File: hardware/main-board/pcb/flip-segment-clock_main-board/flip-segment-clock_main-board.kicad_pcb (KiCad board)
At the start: 2 copper layers, 29.4 x 23 mm, 13 parts, among them IC1 STM32G071CBT6, IC2 DS3231MZ+TRL, IC3 TPS62177DQCR, J1 Barrel_Jack

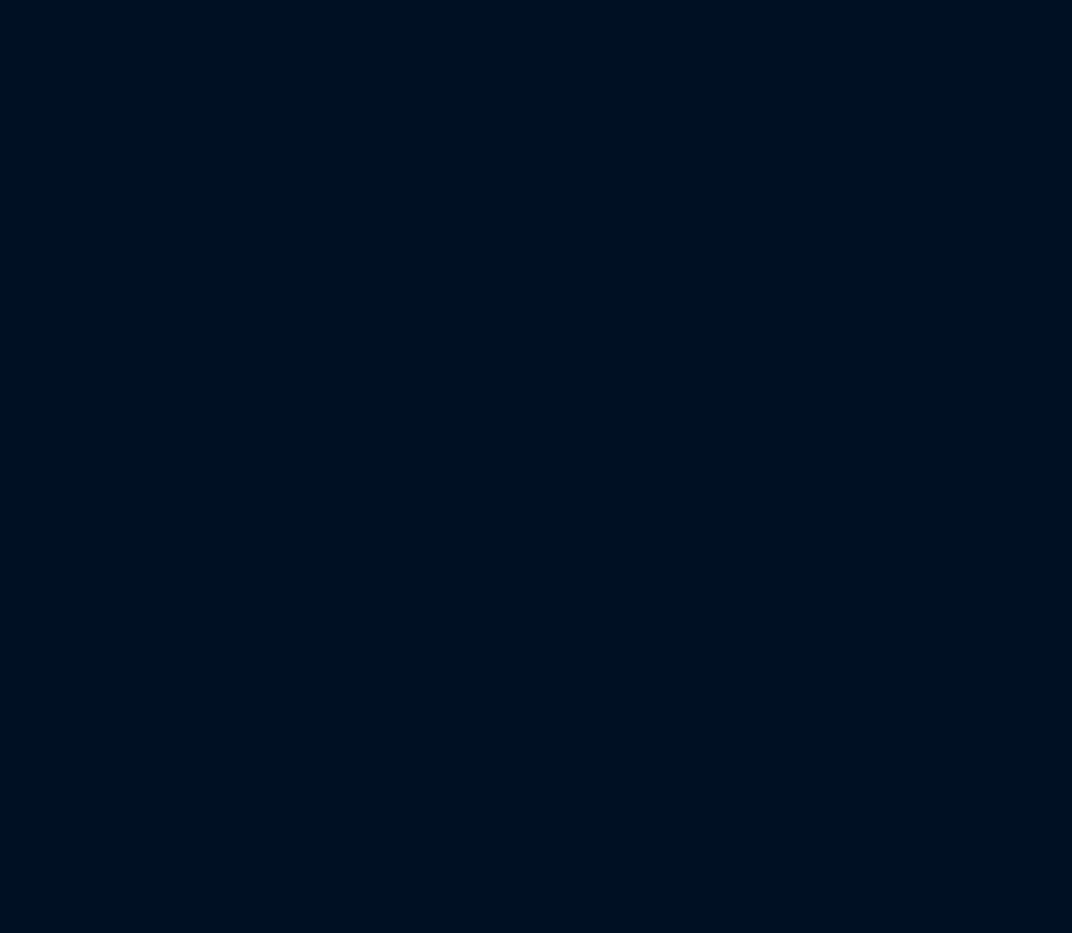
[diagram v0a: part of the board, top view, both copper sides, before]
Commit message: Segment driver update
Continuing refinement of segment driver design, settle on per digit vbb isolation, no overlapping between a3909
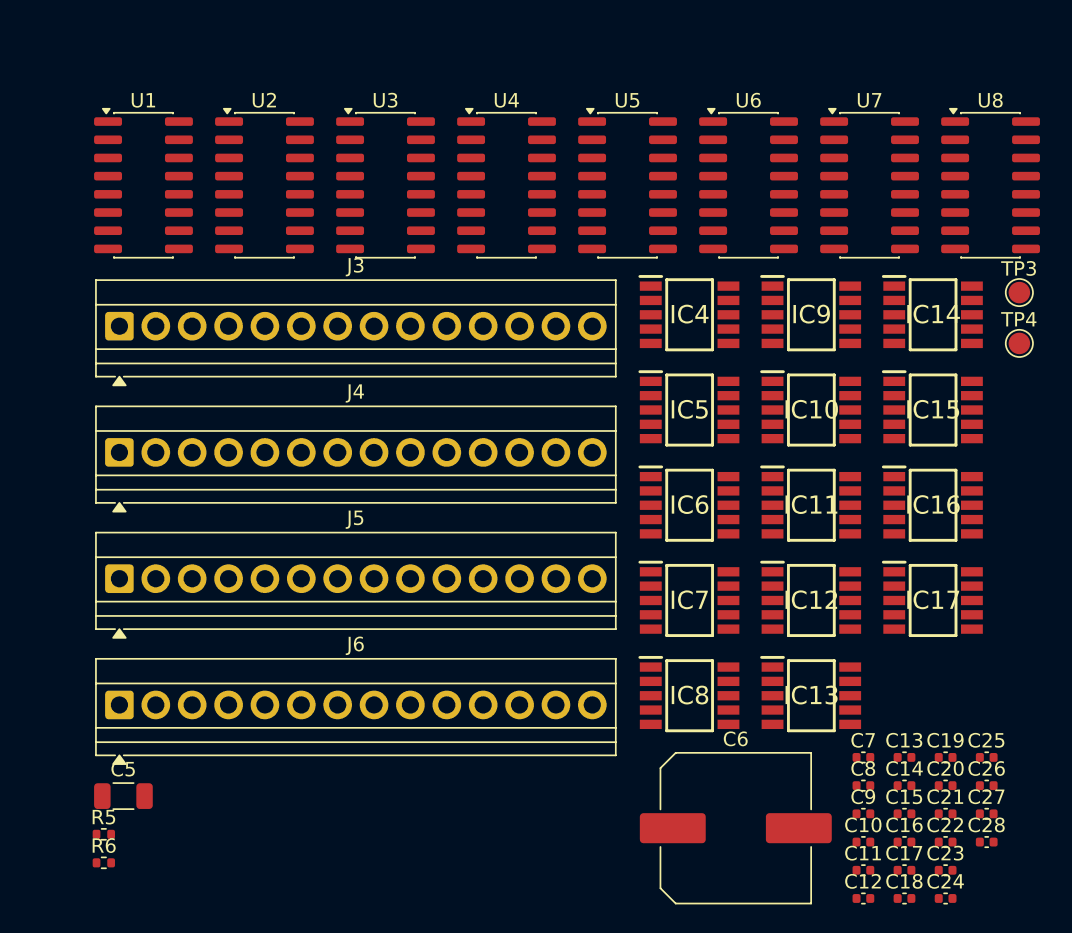
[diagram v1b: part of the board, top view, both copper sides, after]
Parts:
- added C10: 100 nF, Capacitor_SMD:C_0402_1005Metric, F.Cu at (235.7, 118.8)
- added C11: 100 nF, Capacitor_SMD:C_0402_1005Metric, F.Cu at (235.7, 120.7)
- added C12: 100 nF, Capacitor_SMD:C_0402_1005Metric, F.Cu at (235.7, 122.7)
- added C13: 100 nF, Capacitor_SMD:C_0402_1005Metric, F.Cu at (238.5, 112.8)
- added C14: 100 nF, Capacitor_SMD:C_0402_1005Metric, F.Cu at (238.5, 114.8)
- added C15: 100 nF, Capacitor_SMD:C_0402_1005Metric, F.Cu at (238.5, 116.8)
- added C16: 100 nF, Capacitor_SMD:C_0402_1005Metric, F.Cu at (238.5, 118.8)
- added C17: 100 nF, Capacitor_SMD:C_0402_1005Metric, F.Cu at (238.5, 120.7)
- added C18: 100 nF, Capacitor_SMD:C_0402_1005Metric, F.Cu at (238.5, 122.7)
- added C19: 100 nF, Capacitor_SMD:C_0402_1005Metric, F.Cu at (241.4, 112.8)
- added C20: 100 nF, Capacitor_SMD:C_0402_1005Metric, F.Cu at (241.4, 114.8)
- added C21: 100 nF, Capacitor_SMD:C_0402_1005Metric, F.Cu at (241.4, 116.8)
- added C22: 100 nF, Capacitor_SMD:C_0402_1005Metric, F.Cu at (241.4, 118.8)
- added C23: 100 nF, Capacitor_SMD:C_0402_1005Metric, F.Cu at (241.4, 120.7)
- added C24: 100 nF, Capacitor_SMD:C_0402_1005Metric, F.Cu at (241.4, 122.7)
- added C25: 100 nF, Capacitor_SMD:C_0402_1005Metric, F.Cu at (244.3, 112.8)
- added C26: 100 nF, Capacitor_SMD:C_0402_1005Metric, F.Cu at (244.3, 114.8)
- added C27: 100 nF, Capacitor_SMD:C_0402_1005Metric, F.Cu at (244.3, 116.8)
- added C28: 100 nF, Capacitor_SMD:C_0402_1005Metric, F.Cu at (244.3, 118.8)
- added C5: 10 uF, Capacitor_SMD:C_1206_3216Metric, F.Cu at (184.0, 115.5)
- added C6: 560 uF, Capacitor_SMD:C_Elec_10x10.2, F.Cu at (226.8, 117.8)
- added C7: 100 nF, Capacitor_SMD:C_0402_1005Metric, F.Cu at (235.7, 112.8)
- added C8: 100 nF, Capacitor_SMD:C_0402_1005Metric, F.Cu at (235.7, 114.8)
- added C9: 100 nF, Capacitor_SMD:C_0402_1005Metric, F.Cu at (235.7, 116.8)
- added IC10: A3909GLNTR-T, SamacSys_Parts:SOP100P600X175-10N, F.Cu at (232.0, 88.6)
- added IC11: A3909GLNTR-T, SamacSys_Parts:SOP100P600X175-10N, F.Cu at (232.0, 95.2)
- added IC12: A3909GLNTR-T, SamacSys_Parts:SOP100P600X175-10N, F.Cu at (232.0, 101.9)
- added IC13: A3909GLNTR-T, SamacSys_Parts:SOP100P600X175-10N, F.Cu at (232.0, 108.5)
- added IC14: A3909GLNTR-T, SamacSys_Parts:SOP100P600X175-10N, F.Cu at (240.5, 81.9)
- added IC15: A3909GLNTR-T, SamacSys_Parts:SOP100P600X175-10N, F.Cu at (240.5, 88.6)
- added IC16: A3909GLNTR-T, SamacSys_Parts:SOP100P600X175-10N, F.Cu at (240.5, 95.2)
- added IC17: A3909GLNTR-T, SamacSys_Parts:SOP100P600X175-10N, F.Cu at (240.5, 101.9)
- added IC4: A3909GLNTR-T, SamacSys_Parts:SOP100P600X175-10N, F.Cu at (223.5, 81.9)
- added IC5: A3909GLNTR-T, SamacSys_Parts:SOP100P600X175-10N, F.Cu at (223.5, 88.6)
- added IC6: A3909GLNTR-T, SamacSys_Parts:SOP100P600X175-10N, F.Cu at (223.5, 95.2)
- added IC7: A3909GLNTR-T, SamacSys_Parts:SOP100P600X175-10N, F.Cu at (223.5, 101.9)
- added IC8: A3909GLNTR-T, SamacSys_Parts:SOP100P600X175-10N, F.Cu at (223.5, 108.5)
- added IC9: A3909GLNTR-T, SamacSys_Parts:SOP100P600X175-10N, F.Cu at (232.0, 81.9)
- added J3: Digit 1, TerminalBlock:TerminalBlock_Xinya_XY308-2.54-14P_1x14_P2.54mm_Horizontal, F.Cu at (183.7, 82.7)
- added J4: Digit 2, TerminalBlock:TerminalBlock_Xinya_XY308-2.54-14P_1x14_P2.54mm_Horizontal, F.Cu at (183.7, 91.5)
- added J5: Digit 3, TerminalBlock:TerminalBlock_Xinya_XY308-2.54-14P_1x14_P2.54mm_Horizontal, F.Cu at (183.7, 100.4)
- added J6: Digit 4, TerminalBlock:TerminalBlock_Xinya_XY308-2.54-14P_1x14_P2.54mm_Horizontal, F.Cu at (183.7, 109.2)
- added R5: 100K, Resistor_SMD:R_0402_1005Metric, F.Cu at (182.6, 118.2)
- added R6: 100K, Resistor_SMD:R_0402_1005Metric, F.Cu at (182.6, 120.2)
- added TP3: SER, TestPoint:TestPoint_Pad_D1.5mm, F.Cu at (246.6, 80.4)
- added TP4: 12v, TestPoint:TestPoint_Pad_D1.5mm, F.Cu at (246.6, 83.9)
- added U1: 74HC595, Package_SO:SOIC-16_3.9x9.9mm_P1.27mm, F.Cu at (185.4, 72.9)
- added U2: 74HC595, Package_SO:SOIC-16_3.9x9.9mm_P1.27mm, F.Cu at (193.8, 72.9)
- added U3: 74HC595, Package_SO:SOIC-16_3.9x9.9mm_P1.27mm, F.Cu at (202.3, 72.9)
- added U4: 74HC595, Package_SO:SOIC-16_3.9x9.9mm_P1.27mm, F.Cu at (210.7, 72.9)
- added U5: 74HC595, Package_SO:SOIC-16_3.9x9.9mm_P1.27mm, F.Cu at (219.2, 72.9)
- added U6: 74HC595, Package_SO:SOIC-16_3.9x9.9mm_P1.27mm, F.Cu at (227.6, 72.9)
- added U7: 74HC595, Package_SO:SOIC-16_3.9x9.9mm_P1.27mm, F.Cu at (236.1, 72.9)
- added U8: 74HC595, Package_SO:SOIC-16_3.9x9.9mm_P1.27mm, F.Cu at (244.5, 72.9)
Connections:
- net +12V renamed VBB
- net SCL renamed SCL_RTC
- net SDA renamed SDA_RTC

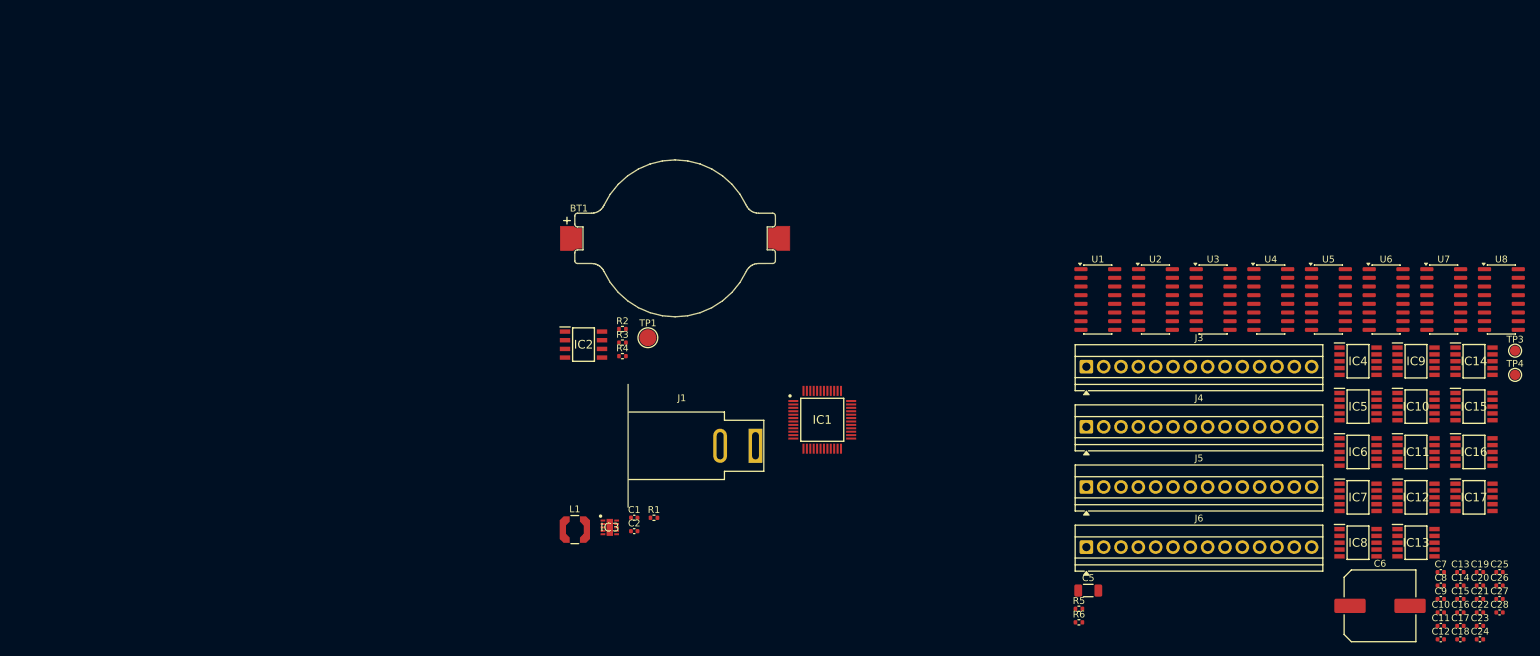
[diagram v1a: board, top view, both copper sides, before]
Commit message: Finalizing design of digit VBB isolation
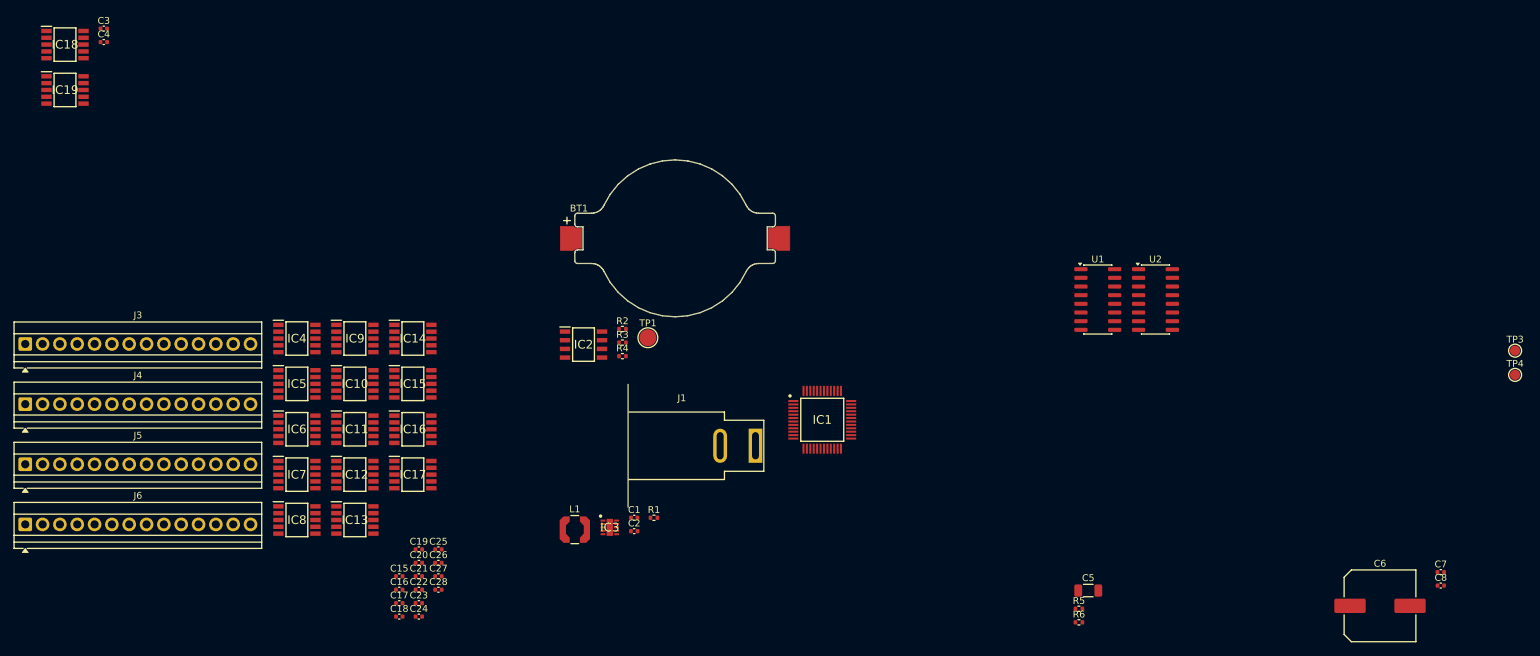
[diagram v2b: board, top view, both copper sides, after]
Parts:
- removed C10, C11, C12, C13, C14, C9: 100 nF, Capacitor_SMD:C_0402_1005Metric
- removed U3, U4, U5, U6, U7, U8: 74HC595, Package_SO:SOIC-16_3.9x9.9mm_P1.27mm
- added C3: 100 nF, Capacitor_SMD:C_0402_1005Metric, F.Cu at (39.7, 33.2)
- added C4: 100 nF, Capacitor_SMD:C_0402_1005Metric, F.Cu at (39.7, 35.1)
- added IC18: A3909GLNTR-T, SamacSys_Parts:SOP100P600X175-10N, F.Cu at (34.0, 35.5)
- added IC19: A3909GLNTR-T, SamacSys_Parts:SOP100P600X175-10N, F.Cu at (34.0, 42.2)
- moved C15 155.6 mm to (83.0, 113.5)
- moved C16 155.6 mm to (83.0, 115.4)
- moved C17 155.6 mm to (83.0, 117.4)
- moved C18 155.6 mm to (83.0, 119.4)
- moved C19 155.6 mm to (85.9, 109.5)
- moved C20 155.6 mm to (85.9, 111.5)
- moved C21 155.6 mm to (85.9, 113.5)
- moved C22 155.6 mm to (85.9, 115.4)
- moved C23 155.6 mm to (85.9, 117.4)
- moved C24 155.6 mm to (85.9, 119.4)
- moved C25 155.6 mm to (88.7, 109.5)
- moved C26 155.6 mm to (88.7, 111.5)
- moved C27 155.6 mm to (88.7, 113.5)
- moved C28 155.6 mm to (88.7, 115.4)
- moved IC10 155.6 mm to (76.5, 85.2)
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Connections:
- C1 pad 2: VBB -> +12V
- C15 pad 2: VBB -> DIG1
- C16 pad 2: VBB -> DIG1
- C17 pad 2: VBB -> DIG1
- C18 pad 2: VBB -> DIG2
- C19 pad 2: VBB -> DIG2
- C20 pad 2: VBB -> DIG2
- C21 pad 2: VBB -> DIG2
- C22 pad 2: VBB -> DIG3
- C23 pad 2: VBB -> DIG3
- C24 pad 2: VBB -> DIG3
- C25 pad 2: VBB -> DIG4
- C26 pad 2: VBB -> DIG4
- C27 pad 2: VBB -> DIG4
- C28 pad 2: VBB -> DIG4
- C5 pad 2: VBB -> +12V
- C6 pad 1: VBB -> +12V
- IC10 pad 1: unconnected-(IC10-IN1-Pad1) -> F3
- IC10 pad 10: unconnected-(IC10-OUT1-Pad10) -> Net-(IC10-OUT1)
- IC10 pad 2: unconnected-(IC10-IN2-Pad2) -> F4
- IC10 pad 3: VBB -> DIG2
- IC10 pad 4: unconnected-(IC10-IN3-Pad4) -> G1
- IC10 pad 5: unconnected-(IC10-IN4-Pad5) -> G2
- IC10 pad 6: unconnected-(IC10-OUT4-Pad6) -> Net-(IC10-OUT4)
- IC10 pad 7: unconnected-(IC10-OUT3-Pad7) -> Net-(IC10-OUT3)
- IC10 pad 9: unconnected-(IC10-OUT2-Pad9) -> Net-(IC10-OUT2)
- IC11 pad 1: unconnected-(IC11-IN1-Pad1) -> A1
- IC11 pad 10: unconnected-(IC11-OUT1-Pad10) -> Net-(IC11-OUT1)
- IC11 pad 2: unconnected-(IC11-IN2-Pad2) -> A2
- IC11 pad 3: VBB -> DIG3
- IC11 pad 4: unconnected-(IC11-IN3-Pad4) -> B3
- IC11 pad 5: unconnected-(IC11-IN4-Pad5) -> B4
- IC11 pad 6: unconnected-(IC11-OUT4-Pad6) -> Net-(IC11-OUT4)
- IC11 pad 7: unconnected-(IC11-OUT3-Pad7) -> Net-(IC11-OUT3)
- IC11 pad 9: unconnected-(IC11-OUT2-Pad9) -> Net-(IC11-OUT2)
- IC12 pad 1: unconnected-(IC12-IN1-Pad1) -> C1
- IC12 pad 10: unconnected-(IC12-OUT1-Pad10) -> Net-(IC12-OUT1)
- IC12 pad 2: unconnected-(IC12-IN2-Pad2) -> C2
- IC12 pad 3: VBB -> DIG3
- IC12 pad 4: unconnected-(IC12-IN3-Pad4) -> D3
- IC12 pad 5: unconnected-(IC12-IN4-Pad5) -> D4
- IC12 pad 6: unconnected-(IC12-OUT4-Pad6) -> Net-(IC12-OUT4)
- IC12 pad 7: unconnected-(IC12-OUT3-Pad7) -> Net-(IC12-OUT3)
- IC12 pad 9: unconnected-(IC12-OUT2-Pad9) -> Net-(IC12-OUT2)
- IC13 pad 1: unconnected-(IC13-IN1-Pad1) -> E1
- IC13 pad 10: unconnected-(IC13-OUT1-Pad10) -> Net-(IC13-OUT1)
- IC13 pad 2: unconnected-(IC13-IN2-Pad2) -> E2
- IC13 pad 3: VBB -> DIG3
- IC13 pad 4: unconnected-(IC13-IN3-Pad4) -> F3
- IC13 pad 5: unconnected-(IC13-IN4-Pad5) -> F4
- IC13 pad 6: unconnected-(IC13-OUT4-Pad6) -> Net-(IC13-OUT4)
- IC13 pad 7: unconnected-(IC13-OUT3-Pad7) -> Net-(IC13-OUT3)
- IC13 pad 9: unconnected-(IC13-OUT2-Pad9) -> Net-(IC13-OUT2)
- IC14 pad 1: unconnected-(IC14-IN1-Pad1) -> GND
- IC14 pad 2: unconnected-(IC14-IN2-Pad2) -> GND
- IC14 pad 3: VBB -> DIG4
- IC14 pad 4: unconnected-(IC14-IN3-Pad4) -> A1
- IC14 pad 5: unconnected-(IC14-IN4-Pad5) -> A2
- IC14 pad 6: unconnected-(IC14-OUT4-Pad6) -> Net-(IC14-OUT4)
- IC14 pad 7: unconnected-(IC14-OUT3-Pad7) -> Net-(IC14-OUT3)
- IC15 pad 1: unconnected-(IC15-IN1-Pad1) -> B3
- IC15 pad 10: unconnected-(IC15-OUT1-Pad10) -> Net-(IC15-OUT1)
- IC15 pad 2: unconnected-(IC15-IN2-Pad2) -> B4
- IC15 pad 3: VBB -> DIG4
- IC15 pad 4: unconnected-(IC15-IN3-Pad4) -> C1
- IC15 pad 5: unconnected-(IC15-IN4-Pad5) -> C2
- IC15 pad 6: unconnected-(IC15-OUT4-Pad6) -> Net-(IC15-OUT4)
- IC15 pad 7: unconnected-(IC15-OUT3-Pad7) -> Net-(IC15-OUT3)
- IC15 pad 9: unconnected-(IC15-OUT2-Pad9) -> Net-(IC15-OUT2)
- IC16 pad 1: unconnected-(IC16-IN1-Pad1) -> D3
- IC16 pad 10: unconnected-(IC16-OUT1-Pad10) -> Net-(IC16-OUT1)
- IC16 pad 2: unconnected-(IC16-IN2-Pad2) -> D4
- IC16 pad 3: VBB -> DIG4
- IC16 pad 4: unconnected-(IC16-IN3-Pad4) -> E1
- IC16 pad 5: unconnected-(IC16-IN4-Pad5) -> E2
- IC16 pad 6: unconnected-(IC16-OUT4-Pad6) -> Net-(IC16-OUT4)
- IC16 pad 7: unconnected-(IC16-OUT3-Pad7) -> Net-(IC16-OUT3)
- IC16 pad 9: unconnected-(IC16-OUT2-Pad9) -> Net-(IC16-OUT2)
- IC17 pad 1: unconnected-(IC17-IN1-Pad1) -> F3
- IC17 pad 10: unconnected-(IC17-OUT1-Pad10) -> Net-(IC17-OUT1)
- IC17 pad 2: unconnected-(IC17-IN2-Pad2) -> F4
- IC17 pad 3: VBB -> DIG4
- IC17 pad 4: unconnected-(IC17-IN3-Pad4) -> G1
- IC17 pad 5: unconnected-(IC17-IN4-Pad5) -> G2
- IC17 pad 6: unconnected-(IC17-OUT4-Pad6) -> Net-(IC17-OUT4)
- IC17 pad 7: unconnected-(IC17-OUT3-Pad7) -> Net-(IC17-OUT3)
- IC17 pad 9: unconnected-(IC17-OUT2-Pad9) -> Net-(IC17-OUT2)
- IC3 pad 2: VBB -> +12V
- IC3 pad 3: VBB -> +12V
- IC4 pad 1: unconnected-(IC4-IN1-Pad1) -> A1
- IC4 pad 10: unconnected-(IC4-OUT1-Pad10) -> Net-(IC4-OUT1)
- IC4 pad 2: unconnected-(IC4-IN2-Pad2) -> A2
- IC4 pad 3: VBB -> DIG1
- IC4 pad 4: unconnected-(IC4-IN3-Pad4) -> B3
- IC4 pad 5: unconnected-(IC4-IN4-Pad5) -> B4
- IC4 pad 6: unconnected-(IC4-OUT4-Pad6) -> Net-(IC4-OUT4)
- IC4 pad 7: unconnected-(IC4-OUT3-Pad7) -> Net-(IC4-OUT3)
- IC4 pad 9: unconnected-(IC4-OUT2-Pad9) -> Net-(IC4-OUT2)
- IC5 pad 1: unconnected-(IC5-IN1-Pad1) -> C1
- IC5 pad 10: unconnected-(IC5-OUT1-Pad10) -> Net-(IC5-OUT1)
- IC5 pad 2: unconnected-(IC5-IN2-Pad2) -> C2
- IC5 pad 3: VBB -> DIG1
- IC5 pad 4: unconnected-(IC5-IN3-Pad4) -> D3
- IC5 pad 5: unconnected-(IC5-IN4-Pad5) -> D4
- IC5 pad 6: unconnected-(IC5-OUT4-Pad6) -> Net-(IC5-OUT4)
- IC5 pad 7: unconnected-(IC5-OUT3-Pad7) -> Net-(IC5-OUT3)
- IC5 pad 9: unconnected-(IC5-OUT2-Pad9) -> Net-(IC5-OUT2)
- IC6 pad 1: unconnected-(IC6-IN1-Pad1) -> E1
- IC6 pad 10: unconnected-(IC6-OUT1-Pad10) -> Net-(IC6-OUT1)
- IC6 pad 2: unconnected-(IC6-IN2-Pad2) -> E2
- IC6 pad 3: VBB -> DIG1
- IC6 pad 4: unconnected-(IC6-IN3-Pad4) -> F3
- IC6 pad 5: unconnected-(IC6-IN4-Pad5) -> F4
- IC6 pad 6: unconnected-(IC6-OUT4-Pad6) -> Net-(IC6-OUT4)
- IC6 pad 7: unconnected-(IC6-OUT3-Pad7) -> Net-(IC6-OUT3)
- IC6 pad 9: unconnected-(IC6-OUT2-Pad9) -> Net-(IC6-OUT2)
- IC7 pad 1: unconnected-(IC7-IN1-Pad1) -> GND
- IC7 pad 2: unconnected-(IC7-IN2-Pad2) -> GND
- IC7 pad 3: VBB -> DIG2
- IC7 pad 4: unconnected-(IC7-IN3-Pad4) -> A1
- IC7 pad 5: unconnected-(IC7-IN4-Pad5) -> A2
- IC7 pad 6: unconnected-(IC7-OUT4-Pad6) -> Net-(IC7-OUT4)
- IC7 pad 7: unconnected-(IC7-OUT3-Pad7) -> Net-(IC7-OUT3)
- IC8 pad 1: unconnected-(IC8-IN1-Pad1) -> B3
- IC8 pad 10: unconnected-(IC8-OUT1-Pad10) -> Net-(IC8-OUT1)
- IC8 pad 2: unconnected-(IC8-IN2-Pad2) -> B4
- IC8 pad 3: VBB -> DIG2
- IC8 pad 4: unconnected-(IC8-IN3-Pad4) -> C1
- IC8 pad 5: unconnected-(IC8-IN4-Pad5) -> C2
- IC8 pad 6: unconnected-(IC8-OUT4-Pad6) -> Net-(IC8-OUT4)
- IC8 pad 7: unconnected-(IC8-OUT3-Pad7) -> Net-(IC8-OUT3)
- IC8 pad 9: unconnected-(IC8-OUT2-Pad9) -> Net-(IC8-OUT2)
- IC9 pad 1: unconnected-(IC9-IN1-Pad1) -> D3
- IC9 pad 10: unconnected-(IC9-OUT1-Pad10) -> Net-(IC9-OUT1)
- IC9 pad 2: unconnected-(IC9-IN2-Pad2) -> D4
- IC9 pad 3: VBB -> DIG2
- IC9 pad 4: unconnected-(IC9-IN3-Pad4) -> E1
- IC9 pad 5: unconnected-(IC9-IN4-Pad5) -> E2
- IC9 pad 6: unconnected-(IC9-OUT4-Pad6) -> Net-(IC9-OUT4)
- IC9 pad 7: unconnected-(IC9-OUT3-Pad7) -> Net-(IC9-OUT3)
- IC9 pad 9: unconnected-(IC9-OUT2-Pad9) -> Net-(IC9-OUT2)
- J1 pad 1: VBB -> +12V
- J3 pad 1: unconnected-(J3-Pin_1-Pad1) -> Net-(IC4-OUT1)
- J3 pad 10: unconnected-(J3-Pin_10-Pad10) -> Net-(IC6-OUT2)
- J3 pad 11: unconnected-(J3-Pin_11-Pad11) -> Net-(IC6-OUT3)
- J3 pad 12: unconnected-(J3-Pin_12-Pad12) -> Net-(IC6-OUT4)
- J3 pad 13: unconnected-(J3-Pin_13-Pad13) -> Net-(IC18-OUT1)
- J3 pad 14: unconnected-(J3-Pin_14-Pad14) -> Net-(IC18-OUT2)
- J3 pad 2: unconnected-(J3-Pin_2-Pad2) -> Net-(IC4-OUT2)
- J3 pad 3: unconnected-(J3-Pin_3-Pad3) -> Net-(IC4-OUT3)
- J3 pad 4: unconnected-(J3-Pin_4-Pad4) -> Net-(IC4-OUT4)
- J3 pad 5: unconnected-(J3-Pin_5-Pad5) -> Net-(IC5-OUT1)
- J3 pad 6: unconnected-(J3-Pin_6-Pad6) -> Net-(IC5-OUT2)
- J3 pad 7: unconnected-(J3-Pin_7-Pad7) -> Net-(IC5-OUT3)
- J3 pad 8: unconnected-(J3-Pin_8-Pad8) -> Net-(IC5-OUT4)
- J3 pad 9: unconnected-(J3-Pin_9-Pad9) -> Net-(IC6-OUT1)
- J4 pad 1: unconnected-(J4-Pin_1-Pad1) -> Net-(IC7-OUT3)
- J4 pad 10: unconnected-(J4-Pin_10-Pad10) -> Net-(IC9-OUT4)
- J4 pad 11: unconnected-(J4-Pin_11-Pad11) -> Net-(IC10-OUT1)
- J4 pad 12: unconnected-(J4-Pin_12-Pad12) -> Net-(IC10-OUT2)
- J4 pad 13: unconnected-(J4-Pin_13-Pad13) -> Net-(IC10-OUT3)
- J4 pad 14: unconnected-(J4-Pin_14-Pad14) -> Net-(IC10-OUT4)
- J4 pad 2: unconnected-(J4-Pin_2-Pad2) -> Net-(IC7-OUT4)
- J4 pad 3: unconnected-(J4-Pin_3-Pad3) -> Net-(IC8-OUT1)
- J4 pad 4: unconnected-(J4-Pin_4-Pad4) -> Net-(IC8-OUT2)
- J4 pad 5: unconnected-(J4-Pin_5-Pad5) -> Net-(IC8-OUT3)
- J4 pad 6: unconnected-(J4-Pin_6-Pad6) -> Net-(IC8-OUT4)
- J4 pad 7: unconnected-(J4-Pin_7-Pad7) -> Net-(IC9-OUT1)
- J4 pad 8: unconnected-(J4-Pin_8-Pad8) -> Net-(IC9-OUT2)
- J4 pad 9: unconnected-(J4-Pin_9-Pad9) -> Net-(IC9-OUT3)
- J5 pad 1: unconnected-(J5-Pin_1-Pad1) -> Net-(IC11-OUT1)
- J5 pad 10: unconnected-(J5-Pin_10-Pad10) -> Net-(IC13-OUT2)
- J5 pad 11: unconnected-(J5-Pin_11-Pad11) -> Net-(IC13-OUT3)
- J5 pad 12: unconnected-(J5-Pin_12-Pad12) -> Net-(IC13-OUT4)
- J5 pad 13: unconnected-(J5-Pin_13-Pad13) -> Net-(IC19-OUT1)
- J5 pad 14: unconnected-(J5-Pin_14-Pad14) -> Net-(IC19-OUT2)
- J5 pad 2: unconnected-(J5-Pin_2-Pad2) -> Net-(IC11-OUT2)
- J5 pad 3: unconnected-(J5-Pin_3-Pad3) -> Net-(IC11-OUT3)
- J5 pad 4: unconnected-(J5-Pin_4-Pad4) -> Net-(IC11-OUT4)
- J5 pad 5: unconnected-(J5-Pin_5-Pad5) -> Net-(IC12-OUT1)
- J5 pad 6: unconnected-(J5-Pin_6-Pad6) -> Net-(IC12-OUT2)
- J5 pad 7: unconnected-(J5-Pin_7-Pad7) -> Net-(IC12-OUT3)
- J5 pad 8: unconnected-(J5-Pin_8-Pad8) -> Net-(IC12-OUT4)
- J5 pad 9: unconnected-(J5-Pin_9-Pad9) -> Net-(IC13-OUT1)
- J6 pad 1: unconnected-(J6-Pin_1-Pad1) -> Net-(IC14-OUT3)
- J6 pad 10: unconnected-(J6-Pin_10-Pad10) -> Net-(IC16-OUT4)
- J6 pad 11: unconnected-(J6-Pin_11-Pad11) -> Net-(IC17-OUT1)
- J6 pad 12: unconnected-(J6-Pin_12-Pad12) -> Net-(IC17-OUT2)
- J6 pad 13: unconnected-(J6-Pin_13-Pad13) -> Net-(IC17-OUT3)
- J6 pad 14: unconnected-(J6-Pin_14-Pad14) -> Net-(IC17-OUT4)
- J6 pad 2: unconnected-(J6-Pin_2-Pad2) -> Net-(IC14-OUT4)
- J6 pad 3: unconnected-(J6-Pin_3-Pad3) -> Net-(IC15-OUT1)
- J6 pad 4: unconnected-(J6-Pin_4-Pad4) -> Net-(IC15-OUT2)
- J6 pad 5: unconnected-(J6-Pin_5-Pad5) -> Net-(IC15-OUT3)
- J6 pad 6: unconnected-(J6-Pin_6-Pad6) -> Net-(IC15-OUT4)
- J6 pad 7: unconnected-(J6-Pin_7-Pad7) -> Net-(IC16-OUT1)
- J6 pad 8: unconnected-(J6-Pin_8-Pad8) -> Net-(IC16-OUT2)
- J6 pad 9: unconnected-(J6-Pin_9-Pad9) -> Net-(IC16-OUT3)
- TP4 pad 1: VBB -> +12V
- U1 pad 1: unconnected-(U1-QB-Pad1) -> A2
- U1 pad 15: unconnected-(U1-QA-Pad15) -> A1
- U1 pad 2: unconnected-(U1-QC-Pad2) -> B3
- U1 pad 3: unconnected-(U1-QD-Pad3) -> B4
- U1 pad 4: unconnected-(U1-QE-Pad4) -> C1
- U1 pad 5: unconnected-(U1-QF-Pad5) -> C2
- U1 pad 6: unconnected-(U1-QG-Pad6) -> D3
- U1 pad 7: unconnected-(U1-QH-Pad7) -> D4
- U2 pad 1: unconnected-(U2-QB-Pad1) -> E2
- U2 pad 15: unconnected-(U2-QA-Pad15) -> E1
- U2 pad 2: unconnected-(U2-QC-Pad2) -> F3
- U2 pad 3: unconnected-(U2-QD-Pad3) -> F4
- U2 pad 4: unconnected-(U2-QE-Pad4) -> G1
- U2 pad 5: unconnected-(U2-QF-Pad5) -> G2
- U2 pad 9: /Segment-Drivers/QH' -> unconnected-(U2-QH'-Pad9)
